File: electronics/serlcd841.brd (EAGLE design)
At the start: 42.4 x 14.2 mm, 13 parts, among them IC1 T841, J1 AVRISP, Q2 16MHz

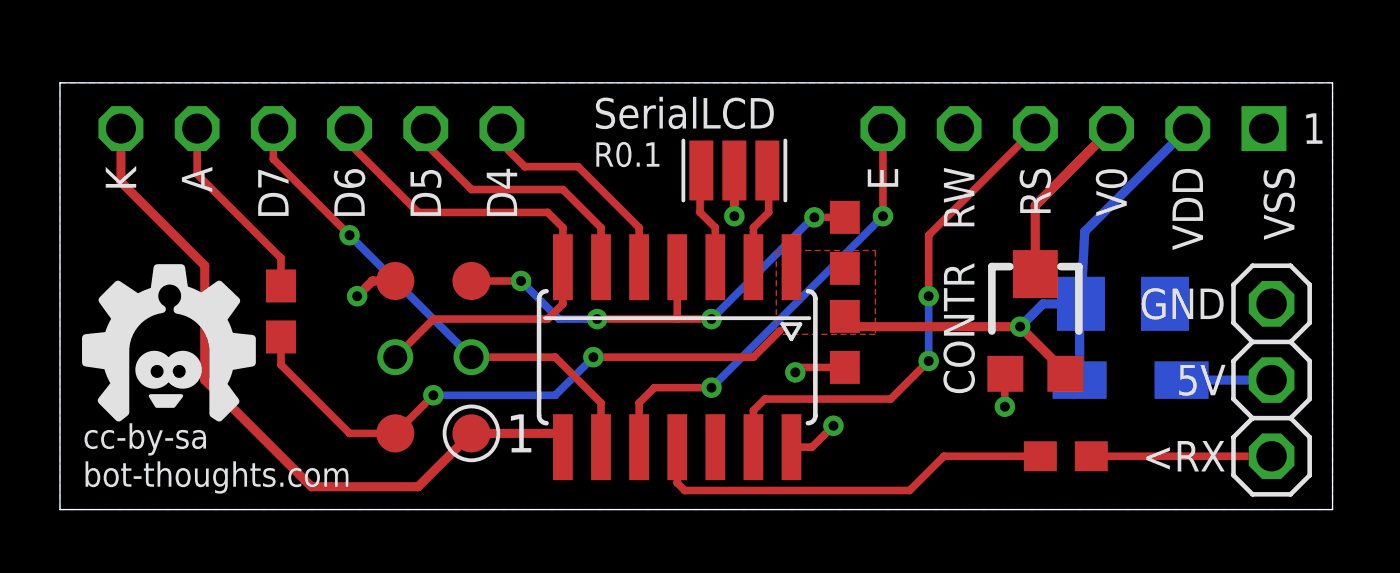
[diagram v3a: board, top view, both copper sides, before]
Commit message: fixed wire/pad clearance issues
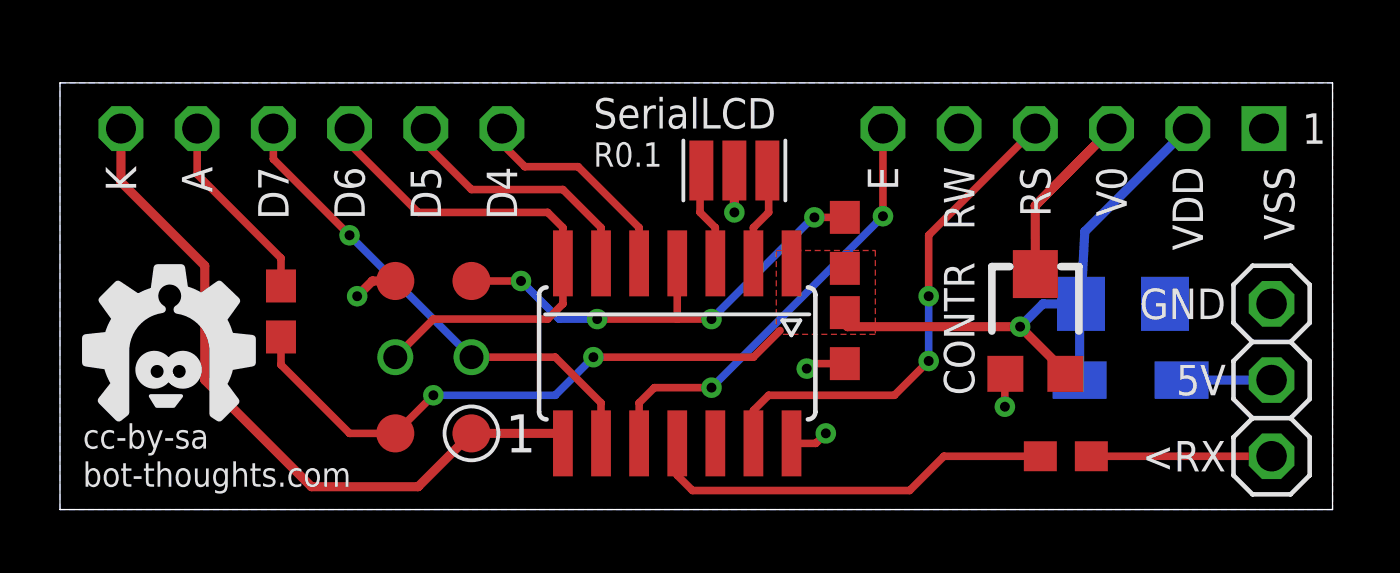
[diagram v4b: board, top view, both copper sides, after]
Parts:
- moved C1 0.13 mm to (26.2, 5.71)
- moved IC1 0.13 mm to (20.6, 5.21)
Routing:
- net GND: track 7.70 -> 6.78 mm
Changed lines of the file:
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@@
 </class>
 </classes>
-<designrules name="LaenPCBOrder">
+<designrules name="LaenPCBOrder *">
 <description language="de">&lt;b&gt;EAGLE Design Rules&lt;/b&gt;
 &lt;p&gt;
@@
 </autorouter>
 <elements>
-<element name="C1" library="bt_rcl" package="0603" value="0.1uF" x="26.162" y="5.588" smashed="yes" rot="R270">
-<attribute name="VALUE" x="26.924" y="5.588" size="0.8128" layer="27" font="vector" ratio="10" rot="R90" align="top-center"/>
+<element name="C1" library="bt_rcl" package="0603" value="0.1uF" x="26.162" y="5.715" smashed="yes" rot="R270">
+<attribute name="VALUE" x="26.924" y="5.715" size="0.8128" layer="27" font="vector" ratio="10" rot="R90" align="top-center"/>
 </element>
 <element name="C2" library="bt_rcl" package="1206" value="10uF" x="35.433" y="6.858" smashed="yes" rot="MR180">
 <attribute name="VALUE" x="35.433" y="8.001" size="0.8128" layer="28" font="vector" ratio="10" rot="MR180" align="top-center"/>
 </element>
-<element name="IC1" library="bt_avr" package="SOIC14N" value="T841" x="20.574" y="5.08" smashed="yes" rot="R180">
-<attribute name="VALUE" x="15.748" y="5.842" size="0.8128" layer="27" font="vector" ratio="10" rot="R90" align="bottom-center"/>
+<element name="IC1" library="bt_avr" package="SOIC14N" value="T841" x="20.574" y="5.207" smashed="yes" rot="R180">
+<attribute name="VALUE" x="15.748" y="5.969" size="0.8128" layer="27" font="vector" ratio="10" rot="R90" align="bottom-center"/>
 </element>
 <element name="J1" library="bt_avr" package="2X3_TP" value="AVRISP" x="12.446" y="5.08" smashed="yes" rot="R180"/>
@@
 <wire x1="21.717" y1="4.064" x2="19.812" y2="4.064" width="0.254" layer="1"/>
 <wire x1="19.812" y1="4.064" x2="19.304" y2="3.556" width="0.254" layer="1"/>
-<wire x1="19.304" y1="3.556" x2="19.304" y2="2.08" width="0.254" layer="1"/>
+<wire x1="19.304" y1="3.556" x2="19.304" y2="2.207" width="0.254" layer="1"/>
 <contactref element="LCD2" pad="E"/>
 <wire x1="27.432" y1="9.779" x2="27.432" y2="12.7" width="0.254" layer="1"/>
@@
 <contactref element="IC1" pad="13"/>
 <contactref element="LCD2" pad="RS"/>
-<wire x1="23.114" y1="2.08" x2="23.114" y2="3.302" width="0.254" layer="1"/>
-<wire x1="23.114" y1="3.302" x2="23.495" y2="3.683" width="0.254" layer="1"/>
-<wire x1="23.495" y1="3.683" x2="27.686" y2="3.683" width="0.254" layer="1"/>
-<wire x1="27.686" y1="3.683" x2="28.956" y2="4.953" width="0.254" layer="1"/>
+<wire x1="23.114" y1="2.207" x2="23.114" y2="3.302" width="0.254" layer="1"/>
+<wire x1="23.114" y1="3.302" x2="23.622" y2="3.81" width="0.254" layer="1"/>
+<wire x1="23.622" y1="3.81" x2="27.813" y2="3.81" width="0.254" layer="1"/>
+<wire x1="27.813" y1="3.81" x2="28.956" y2="4.953" width="0.254" layer="1"/>
 <via x="28.956" y="4.953" extent="1-16" drill="0.3302"/>
 <wire x1="28.956" y1="4.953" x2="28.956" y2="7.112" width="0.254" layer="16"/>
@@
 <contactref element="R5" pad="2"/>
 <wire x1="29.464" y1="1.778" x2="32.678" y2="1.778" width="0.254" layer="1"/>
-<wire x1="20.574" y1="2.08" x2="20.574" y2="0.889" width="0.254" layer="1"/>
-<wire x1="20.574" y1="0.889" x2="20.828" y2="0.635" width="0.254" layer="1"/>
-<wire x1="20.828" y1="0.635" x2="28.321" y2="0.635" width="0.254" layer="1"/>
+<wire x1="20.574" y1="2.207" x2="20.574" y2="1.143" width="0.254" layer="1"/>
+<wire x1="20.574" y1="1.143" x2="21.082" y2="0.635" width="0.254" layer="1"/>
+<wire x1="21.082" y1="0.635" x2="28.321" y2="0.635" width="0.254" layer="1"/>
 <wire x1="28.321" y1="0.635" x2="29.464" y2="1.778" width="0.254" layer="1"/>
 </signal>
@@
 <wire x1="13.716" y1="5.08" x2="16.51" y2="5.08" width="0.254" layer="1"/>
 <wire x1="16.51" y1="5.08" x2="18.034" y2="3.556" width="0.254" layer="1"/>
-<wire x1="18.034" y1="3.556" x2="18.034" y2="2.08" width="0.254" layer="1"/>
+<wire x1="18.034" y1="3.556" x2="18.034" y2="2.207" width="0.254" layer="1"/>
 <wire x1="7.112" y1="12.7" x2="7.112" y2="11.684" width="0.254" layer="1"/>
 <wire x1="7.112" y1="11.684" x2="9.652" y2="9.144" width="0.254" layer="1"/>
@@
 <wire x1="11.938" y1="9.906" x2="16.256" y2="9.906" width="0.254" layer="1"/>
 <wire x1="16.256" y1="9.906" x2="16.764" y2="9.398" width="0.254" layer="1"/>
-<wire x1="16.764" y1="9.398" x2="16.764" y2="8.08" width="0.254" layer="1"/>
+<wire x1="16.764" y1="9.398" x2="16.764" y2="8.207" width="0.254" layer="1"/>
 <wire x1="11.176" y1="5.08" x2="12.446" y2="6.35" width="0.254" layer="1"/>
 <wire x1="12.446" y1="6.35" x2="16.256" y2="6.35" width="0.254" layer="1"/>
 <wire x1="16.256" y1="6.35" x2="16.764" y2="6.858" width="0.254" layer="1"/>
-<wire x1="16.764" y1="6.858" x2="16.764" y2="8.08" width="0.254" layer="1"/>
+<wire x1="16.764" y1="6.858" x2="16.764" y2="8.207" width="0.254" layer="1"/>
 <contactref element="LCD2" pad="D6"/>
 </signal>
@@
 <wire x1="13.716" y1="10.668" x2="16.764" y2="10.668" width="0.254" layer="1"/>
 <wire x1="16.764" y1="10.668" x2="18.034" y2="9.398" width="0.254" layer="1"/>
-<wire x1="18.034" y1="9.398" x2="18.034" y2="8.08" width="0.254" layer="1"/>
+<wire x1="18.034" y1="9.398" x2="18.034" y2="8.207" width="0.254" layer="1"/>
 <contactref element="LCD2" pad="D5"/>
 <wire x1="12.188" y1="12.196" x2="12.188" y2="12.696" width="0.254" layer="1"/>
@@
 <wire x1="17.78" y1="5.08" x2="23.114" y2="5.08" width="0.254" layer="1"/>
 <wire x1="23.114" y1="5.08" x2="24.003" y2="5.969" width="0.254" layer="1"/>
-<wire x1="26.162" y1="6.438" x2="26.25" y2="6.096" width="0.3048" layer="1"/>
+<wire x1="26.162" y1="6.565" x2="26.25" y2="6.096" width="0.3048" layer="1"/>
 <wire x1="26.25" y1="6.096" x2="32.004" y2="6.096" width="0.3048" layer="1"/>
 <wire x1="32.004" y1="6.096" x2="33.512" y2="4.588" width="0.3048" layer="1"/>
@@
 <wire x1="10.414" y1="7.62" x2="9.906" y2="7.112" width="0.3048" layer="1"/>
 <via x="9.906" y="7.112" extent="1-16" drill="0.3302"/>
-<via x="22.479" y="9.779" extent="1-16" drill="0.3302"/>
+<via x="22.479" y="9.906" extent="1-16" drill="0.3302"/>
 <via x="31.496" y="3.429" extent="1-16" drill="0.3302"/>
-<via x="25.781" y="2.794" extent="1-16" drill="0.3302"/>
-<wire x1="24.384" y1="2.08" x2="25.067" y2="2.08" width="0.254" layer="1"/>
-<wire x1="25.067" y1="2.08" x2="25.781" y2="2.794" width="0.254" layer="1"/>
-<wire x1="26.162" y1="4.738" x2="24.677" y2="4.738" width="0.254" layer="1"/>
-<wire x1="24.677" y1="4.738" x2="24.511" y2="4.572" width="0.254" layer="1"/>
-<via x="24.511" y="4.572" extent="1-16" drill="0.3302"/>
+<via x="25.527" y="2.54" extent="1-16" drill="0.3302"/>
+<wire x1="24.384" y1="2.207" x2="25.194" y2="2.207" width="0.254" layer="1"/>
+<wire x1="25.194" y1="2.207" x2="25.527" y2="2.54" width="0.254" layer="1"/>
+<wire x1="26.162" y1="4.865" x2="25.058" y2="4.865" width="0.254" layer="1"/>
+<wire x1="25.058" y1="4.865" x2="24.892" y2="4.699" width="0.254" layer="1"/>
+<via x="24.892" y="4.699" extent="1-16" drill="0.3302"/>
 <wire x1="31.496" y1="3.429" x2="31.496" y2="4.509" width="0.254" layer="1"/>
 <wire x1="31.496" y1="4.509" x2="31.512" y2="4.525" width="0.254" layer="1"/>
-<wire x1="22.479" y1="11.303" x2="22.479" y2="9.779" width="0.3048" layer="1"/>
+<wire x1="22.479" y1="11.303" x2="22.479" y2="9.906" width="0.3048" layer="1"/>
 </signal>
 <signal name="RESET">
@@
 <wire x1="16.637" y1="6.35" x2="17.907" y2="6.35" width="0.254" layer="16"/>
 <wire x1="17.907" y1="6.35" x2="20.574" y2="6.35" width="0.254" layer="1"/>
-<wire x1="20.574" y1="6.35" x2="20.574" y2="8.08" width="0.254" layer="1"/>
+<wire x1="20.574" y1="6.35" x2="20.574" y2="8.207" width="0.254" layer="1"/>
 <via x="17.907" y="6.35" extent="1-16" drill="0.3302"/>
 <via x="21.717" y="6.35" extent="1-16" drill="0.3302"/>
@@
 <wire x1="8.382" y1="0.762" x2="11.938" y2="0.762" width="0.3048" layer="1"/>
 <wire x1="11.938" y1="0.762" x2="13.716" y2="2.54" width="0.3048" layer="1"/>
-<wire x1="16.764" y1="2.08" x2="16.764" y2="2.54" width="0.3048" layer="1"/>
+<wire x1="16.764" y1="2.207" x2="16.764" y2="2.54" width="0.3048" layer="1"/>
 <wire x1="16.764" y1="2.54" x2="13.716" y2="2.54" width="0.3048" layer="1"/>
 </signal>
@@
 <wire x1="15.494" y1="11.43" x2="17.272" y2="11.43" width="0.254" layer="1"/>
 <wire x1="17.272" y1="11.43" x2="19.304" y2="9.398" width="0.254" layer="1"/>
-<wire x1="19.304" y1="9.398" x2="19.304" y2="8.08" width="0.254" layer="1"/>
+<wire x1="19.304" y1="9.398" x2="19.304" y2="8.207" width="0.254" layer="1"/>
 <contactref element="LCD2" pad="D4"/>
 <wire x1="14.728" y1="12.196" x2="14.728" y2="12.696" width="0.254" layer="1"/>
@@
 <contactref element="IC1" pad="2"/>
 <contactref element="Q2" pad="X2"/>
-<wire x1="23.114" y1="8.08" x2="23.114" y2="9.398" width="0.254" layer="1"/>
+<wire x1="23.114" y1="8.207" x2="23.114" y2="9.398" width="0.254" layer="1"/>
 <wire x1="23.114" y1="9.398" x2="23.622" y2="9.906" width="0.254" layer="1"/>
 <wire x1="23.622" y1="9.906" x2="23.622" y2="11.26" width="0.254" layer="1"/>
@@
 <contactref element="IC1" pad="3"/>
 <contactref element="Q2" pad="X1"/>
-<wire x1="21.844" y1="8.08" x2="21.844" y2="9.398" width="0.254" layer="1"/>
+<wire x1="21.844" y1="8.207" x2="21.844" y2="9.398" width="0.254" layer="1"/>
 <wire x1="21.844" y1="9.398" x2="21.336" y2="9.906" width="0.254" layer="1"/>
 <wire x1="21.336" y1="9.906" x2="21.336" y2="11.26" width="0.254" layer="1"/>

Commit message: i don't remember :(
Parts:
- added Q1: 2n3904, bt_transistor:SOT-23
- added R1: 10K, bt_rcl:0603
- J1: device bt_avr:2X3_TP -> bt_avr:CON6P2R
- moved R5 5.47 mm to (28.1, 2.16)
- moved D1 2.70 mm to (33.7, 2.54), flipped to the top, turned to 0 degrees
- moved VR1 1.77 mm to (30.9, 6.99)
- moved U$6 1.53 mm to (3.43, 1.27)
- moved C2 0.85 mm to (34.7, 6.48), flipped to the top, turned to 270 degrees
- moved J1 0.63 mm to (11.8, 5.08), turned to 90 degrees
- moved JP1 0.38 mm to (40.8, 4.32)
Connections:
- new net N$4: Q1.3, R1.2
- new net N$5: LCD2.K, Q1.1
- net GND: now also Q1.2
- net PA5: now also R1.1; no longer LCD2.K
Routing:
- net PA5: track 24.0 -> 10.6 mm
- net N$4: track 0.00 -> 6.71 mm
- net RXI: track 6.01 -> 12.0 mm, vias 0 -> 1
- net RX: track 13.9 -> 8.55 mm
- net VCC: track 40.5 -> 44.1 mm, vias 3 -> 1
- net N$1: track 3.00 -> 6.15 mm
- net N$5: track 0.00 -> 3.00 mm
- net VO: track 9.51 -> 6.55 mm
- net RS: track 16.8 -> 14.6 mm
- net PA4: track 16.7 -> 18.1 mm
- net RESET: track 16.5 -> 17.1 mm, vias 4 -> 3
- net PA6: track 17.6 -> 18.3 mm
- net GND: track 6.78 -> 6.56 mm, vias 5 -> 6
- removed copper zone on layer 1, net VCC
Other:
- board text added: "CONT"
- board text added: "R0.2"
- board text removed: "CONTR"
- board text removed: "R0.1"
